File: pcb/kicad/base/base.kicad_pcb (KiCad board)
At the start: 2 copper layers, 58 parts, among them P1 J-Link SWD, P10 CONN_01X02, P11 CONN_01X02, P2 SMA, P3 CONN_01X02, P4 USB Micro B, P5 Button, P6 Button, P7 Button, P8 Button, P9 Button, Q1 IRLML2502, U1 SAMB11G18A-edit, U2 XBee-PRO_900HP, Y1 32.768kHz, Y2 26MHz

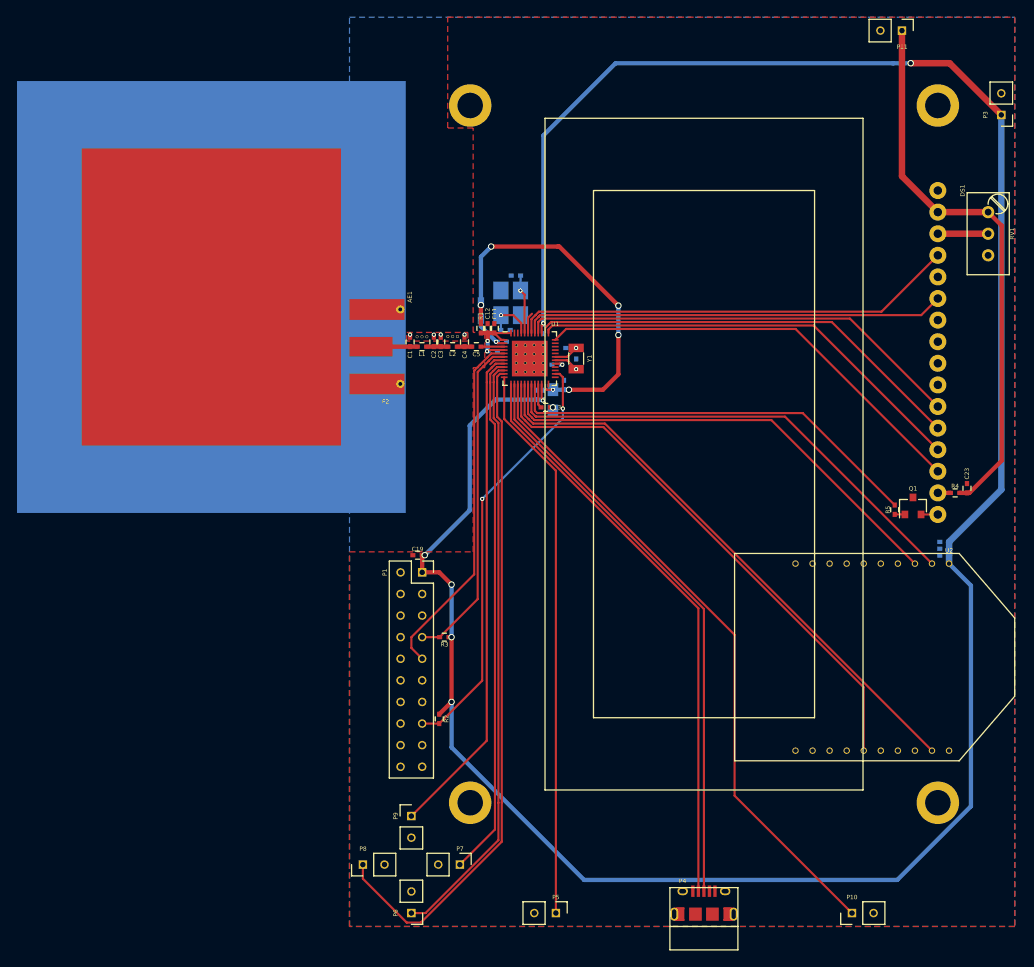
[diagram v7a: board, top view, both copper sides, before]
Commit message: Add ground stitch vias and silk identifiers
Base station layout is finished, and artwork has been generated.
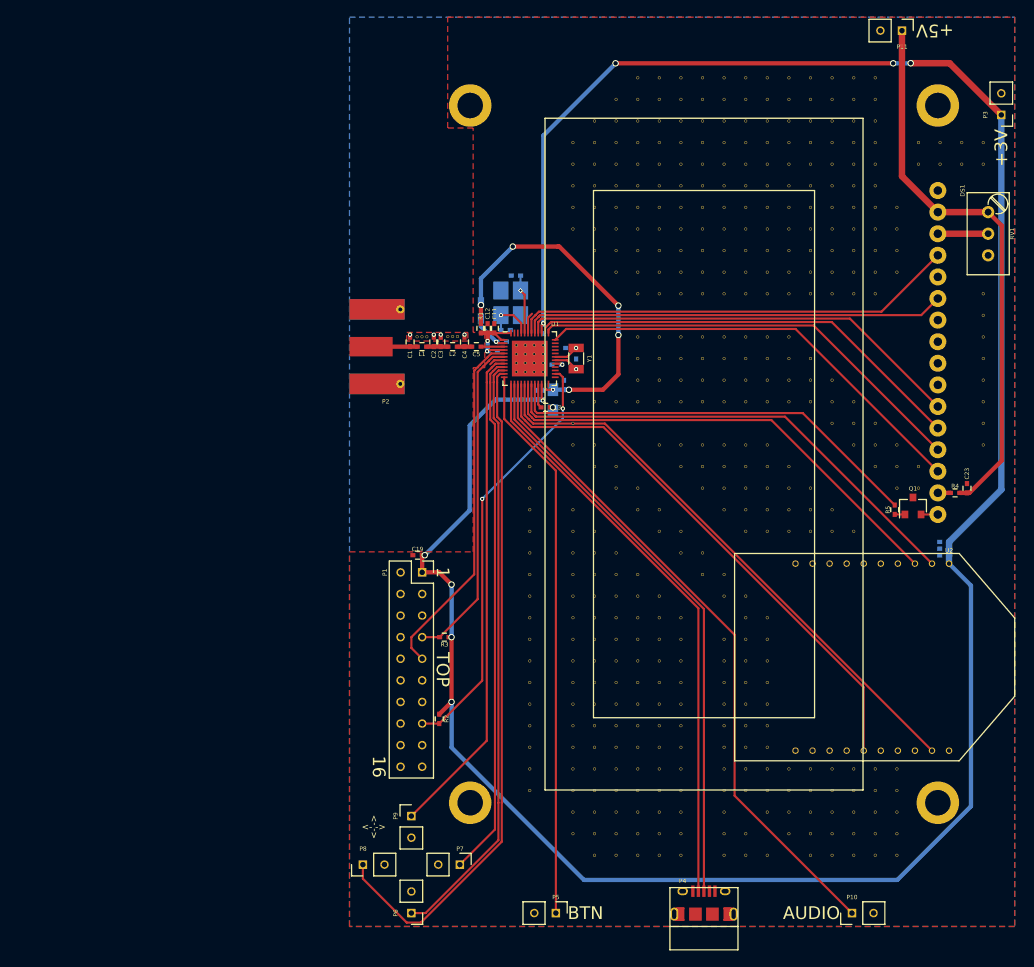
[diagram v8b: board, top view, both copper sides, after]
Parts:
- removed AE1: Antenna_Shield, Antennas:Patch_Antenna_2.4GHz
- added REF**: Via_Stitch_Dia0.356mm_Drill0.254mm, Misc:Via_Stitch_Dia0.356mm_Drill0.254mm, F.Cu at (183.4, 45.3)
- added REF**: Via_Stitch_Dia0.356mm_Drill0.254mm, Misc:Via_Stitch_Dia0.356mm_Drill0.254mm, F.Cu at (183.4, 63.1)
- added REF**: Via_Stitch_Dia0.356mm_Drill0.254mm, Misc:Via_Stitch_Dia0.356mm_Drill0.254mm, F.Cu at (135.1, 88.5)
- added REF**: Via_Stitch_Dia0.356mm_Drill0.254mm, Misc:Via_Stitch_Dia0.356mm_Drill0.254mm, F.Cu at (135.1, 116.5)
- added REF**: Via_Stitch_Dia0.356mm_Drill0.254mm, Misc:Via_Stitch_Dia0.356mm_Drill0.254mm, F.Cu at (135.1, 119.0)
- added REF**: Via_Stitch_Dia0.356mm_Drill0.254mm, Misc:Via_Stitch_Dia0.356mm_Drill0.254mm, F.Cu at (135.1, 121.5)
- added REF**: Via_Stitch_Dia0.356mm_Drill0.254mm, Misc:Via_Stitch_Dia0.356mm_Drill0.254mm, F.Cu at (145.3, 121.5)
- added REF**: Via_Stitch_Dia0.356mm_Drill0.254mm, Misc:Via_Stitch_Dia0.356mm_Drill0.254mm, F.Cu at (142.7, 121.5)
- added REF**: Via_Stitch_Dia0.356mm_Drill0.254mm, Misc:Via_Stitch_Dia0.356mm_Drill0.254mm, F.Cu at (137.6, 121.5)
- added REF**: Via_Stitch_Dia0.356mm_Drill0.254mm, Misc:Via_Stitch_Dia0.356mm_Drill0.254mm, F.Cu at (140.2, 121.5)
- added REF**: Via_Stitch_Dia0.356mm_Drill0.254mm, Misc:Via_Stitch_Dia0.356mm_Drill0.254mm, F.Cu at (145.3, 119.0)
- added REF**: Via_Stitch_Dia0.356mm_Drill0.254mm, Misc:Via_Stitch_Dia0.356mm_Drill0.254mm, F.Cu at (142.7, 119.0)
- added REF**: Via_Stitch_Dia0.356mm_Drill0.254mm, Misc:Via_Stitch_Dia0.356mm_Drill0.254mm, F.Cu at (183.4, 73.3)
- added REF**: Via_Stitch_Dia0.356mm_Drill0.254mm, Misc:Via_Stitch_Dia0.356mm_Drill0.254mm, F.Cu at (137.6, 119.0)
- added REF**: Via_Stitch_Dia0.356mm_Drill0.254mm, Misc:Via_Stitch_Dia0.356mm_Drill0.254mm, F.Cu at (140.2, 119.0)
- added REF**: Via_Stitch_Dia0.356mm_Drill0.254mm, Misc:Via_Stitch_Dia0.356mm_Drill0.254mm, F.Cu at (140.2, 116.5)
- added REF**: Via_Stitch_Dia0.356mm_Drill0.254mm, Misc:Via_Stitch_Dia0.356mm_Drill0.254mm, F.Cu at (137.6, 116.5)
- added REF**: Via_Stitch_Dia0.356mm_Drill0.254mm, Misc:Via_Stitch_Dia0.356mm_Drill0.254mm, F.Cu at (142.7, 116.5)
- added REF**: Via_Stitch_Dia0.356mm_Drill0.254mm, Misc:Via_Stitch_Dia0.356mm_Drill0.254mm, F.Cu at (145.3, 116.5)
- added REF**: Via_Stitch_Dia0.356mm_Drill0.254mm, Misc:Via_Stitch_Dia0.356mm_Drill0.254mm, F.Cu at (147.8, 116.5)
- added REF**: Via_Stitch_Dia0.356mm_Drill0.254mm, Misc:Via_Stitch_Dia0.356mm_Drill0.254mm, F.Cu at (147.8, 119.0)
- added REF**: Via_Stitch_Dia0.356mm_Drill0.254mm, Misc:Via_Stitch_Dia0.356mm_Drill0.254mm, F.Cu at (147.8, 121.5)
- added REF**: Via_Stitch_Dia0.356mm_Drill0.254mm, Misc:Via_Stitch_Dia0.356mm_Drill0.254mm, F.Cu at (147.8, 129.2)
- added REF**: Via_Stitch_Dia0.356mm_Drill0.254mm, Misc:Via_Stitch_Dia0.356mm_Drill0.254mm, F.Cu at (183.4, 75.8)
- added REF**: Via_Stitch_Dia0.356mm_Drill0.254mm, Misc:Via_Stitch_Dia0.356mm_Drill0.254mm, F.Cu at (147.8, 126.6)
- added REF**: Via_Stitch_Dia0.356mm_Drill0.254mm, Misc:Via_Stitch_Dia0.356mm_Drill0.254mm, F.Cu at (147.8, 124.1)
- added REF**: Via_Stitch_Dia0.356mm_Drill0.254mm, Misc:Via_Stitch_Dia0.356mm_Drill0.254mm, F.Cu at (145.3, 124.1)
- added REF**: Via_Stitch_Dia0.356mm_Drill0.254mm, Misc:Via_Stitch_Dia0.356mm_Drill0.254mm, F.Cu at (142.7, 124.1)
- added REF**: Via_Stitch_Dia0.356mm_Drill0.254mm, Misc:Via_Stitch_Dia0.356mm_Drill0.254mm, F.Cu at (137.6, 124.1)
- added REF**: Via_Stitch_Dia0.356mm_Drill0.254mm, Misc:Via_Stitch_Dia0.356mm_Drill0.254mm, F.Cu at (140.2, 124.1)
- added REF**: Via_Stitch_Dia0.356mm_Drill0.254mm, Misc:Via_Stitch_Dia0.356mm_Drill0.254mm, F.Cu at (140.2, 126.6)
- added REF**: Via_Stitch_Dia0.356mm_Drill0.254mm, Misc:Via_Stitch_Dia0.356mm_Drill0.254mm, F.Cu at (137.6, 126.6)
- added REF**: Via_Stitch_Dia0.356mm_Drill0.254mm, Misc:Via_Stitch_Dia0.356mm_Drill0.254mm, F.Cu at (142.7, 126.6)
- added REF**: Via_Stitch_Dia0.356mm_Drill0.254mm, Misc:Via_Stitch_Dia0.356mm_Drill0.254mm, F.Cu at (145.3, 126.6)
- added REF**: Via_Stitch_Dia0.356mm_Drill0.254mm, Misc:Via_Stitch_Dia0.356mm_Drill0.254mm, F.Cu at (183.4, 70.7)
- added REF**: Via_Stitch_Dia0.356mm_Drill0.254mm, Misc:Via_Stitch_Dia0.356mm_Drill0.254mm, F.Cu at (140.2, 129.2)
- added REF**: Via_Stitch_Dia0.356mm_Drill0.254mm, Misc:Via_Stitch_Dia0.356mm_Drill0.254mm, F.Cu at (137.6, 129.2)
- added REF**: Via_Stitch_Dia0.356mm_Drill0.254mm, Misc:Via_Stitch_Dia0.356mm_Drill0.254mm, F.Cu at (142.7, 129.2)
- added REF**: Via_Stitch_Dia0.356mm_Drill0.254mm, Misc:Via_Stitch_Dia0.356mm_Drill0.254mm, F.Cu at (145.3, 129.2)
- added REF**: Via_Stitch_Dia0.356mm_Drill0.254mm, Misc:Via_Stitch_Dia0.356mm_Drill0.254mm, F.Cu at (135.1, 126.6)
- added REF**: Via_Stitch_Dia0.356mm_Drill0.254mm, Misc:Via_Stitch_Dia0.356mm_Drill0.254mm, F.Cu at (135.1, 124.1)
- added REF**: Via_Stitch_Dia0.356mm_Drill0.254mm, Misc:Via_Stitch_Dia0.356mm_Drill0.254mm, F.Cu at (135.1, 108.8)
- added REF**: Via_Stitch_Dia0.356mm_Drill0.254mm, Misc:Via_Stitch_Dia0.356mm_Drill0.254mm, F.Cu at (135.1, 111.4)
- added REF**: Via_Stitch_Dia0.356mm_Drill0.254mm, Misc:Via_Stitch_Dia0.356mm_Drill0.254mm, F.Cu at (135.1, 113.9)
- added REF**: Via_Stitch_Dia0.356mm_Drill0.254mm, Misc:Via_Stitch_Dia0.356mm_Drill0.254mm, F.Cu at (145.3, 113.9)
- added REF**: Via_Stitch_Dia0.356mm_Drill0.254mm, Misc:Via_Stitch_Dia0.356mm_Drill0.254mm, F.Cu at (183.4, 68.2)
- added REF**: Via_Stitch_Dia0.356mm_Drill0.254mm, Misc:Via_Stitch_Dia0.356mm_Drill0.254mm, F.Cu at (142.7, 113.9)
- added REF**: Via_Stitch_Dia0.356mm_Drill0.254mm, Misc:Via_Stitch_Dia0.356mm_Drill0.254mm, F.Cu at (137.6, 113.9)
- added REF**: Via_Stitch_Dia0.356mm_Drill0.254mm, Misc:Via_Stitch_Dia0.356mm_Drill0.254mm, F.Cu at (140.2, 113.9)
- added REF**: Via_Stitch_Dia0.356mm_Drill0.254mm, Misc:Via_Stitch_Dia0.356mm_Drill0.254mm, F.Cu at (145.3, 111.4)
- added REF**: Via_Stitch_Dia0.356mm_Drill0.254mm, Misc:Via_Stitch_Dia0.356mm_Drill0.254mm, F.Cu at (142.7, 111.4)
- added REF**: Via_Stitch_Dia0.356mm_Drill0.254mm, Misc:Via_Stitch_Dia0.356mm_Drill0.254mm, F.Cu at (137.6, 111.4)
- added REF**: Via_Stitch_Dia0.356mm_Drill0.254mm, Misc:Via_Stitch_Dia0.356mm_Drill0.254mm, F.Cu at (140.2, 111.4)
- added REF**: Via_Stitch_Dia0.356mm_Drill0.254mm, Misc:Via_Stitch_Dia0.356mm_Drill0.254mm, F.Cu at (140.2, 108.8)
- added REF**: Via_Stitch_Dia0.356mm_Drill0.254mm, Misc:Via_Stitch_Dia0.356mm_Drill0.254mm, F.Cu at (137.6, 108.8)
- added REF**: Via_Stitch_Dia0.356mm_Drill0.254mm, Misc:Via_Stitch_Dia0.356mm_Drill0.254mm, F.Cu at (142.7, 108.8)
- added REF**: Via_Stitch_Dia0.356mm_Drill0.254mm, Misc:Via_Stitch_Dia0.356mm_Drill0.254mm, F.Cu at (183.4, 78.4)
- added REF**: Via_Stitch_Dia0.356mm_Drill0.254mm, Misc:Via_Stitch_Dia0.356mm_Drill0.254mm, F.Cu at (145.3, 108.8)
- added REF**: Via_Stitch_Dia0.356mm_Drill0.254mm, Misc:Via_Stitch_Dia0.356mm_Drill0.254mm, F.Cu at (147.8, 108.8)
- added REF**: Via_Stitch_Dia0.356mm_Drill0.254mm, Misc:Via_Stitch_Dia0.356mm_Drill0.254mm, F.Cu at (147.8, 111.4)
- added REF**: Via_Stitch_Dia0.356mm_Drill0.254mm, Misc:Via_Stitch_Dia0.356mm_Drill0.254mm, F.Cu at (147.8, 113.9)
- added REF**: Via_Stitch_Dia0.356mm_Drill0.254mm, Misc:Via_Stitch_Dia0.356mm_Drill0.254mm, F.Cu at (147.8, 106.3)
- added REF**: Via_Stitch_Dia0.356mm_Drill0.254mm, Misc:Via_Stitch_Dia0.356mm_Drill0.254mm, F.Cu at (147.8, 103.8)
- added REF**: Via_Stitch_Dia0.356mm_Drill0.254mm, Misc:Via_Stitch_Dia0.356mm_Drill0.254mm, F.Cu at (147.8, 101.2)
- added REF**: Via_Stitch_Dia0.356mm_Drill0.254mm, Misc:Via_Stitch_Dia0.356mm_Drill0.254mm, F.Cu at (135.1, 78.4)
- added REF**: Via_Stitch_Dia0.356mm_Drill0.254mm, Misc:Via_Stitch_Dia0.356mm_Drill0.254mm, F.Cu at (135.1, 80.9)
- added REF**: Via_Stitch_Dia0.356mm_Drill0.254mm, Misc:Via_Stitch_Dia0.356mm_Drill0.254mm, F.Cu at (137.6, 80.9)
- added REF**: Via_Stitch_Dia0.356mm_Drill0.254mm, Misc:Via_Stitch_Dia0.356mm_Drill0.254mm, F.Cu at (183.4, 80.9)
- added REF**: Via_Stitch_Dia0.356mm_Drill0.254mm, Misc:Via_Stitch_Dia0.356mm_Drill0.254mm, F.Cu at (137.6, 83.4)
- added REF**: Via_Stitch_Dia0.356mm_Drill0.254mm, Misc:Via_Stitch_Dia0.356mm_Drill0.254mm, F.Cu at (142.7, 88.5)
- added REF**: Via_Stitch_Dia0.356mm_Drill0.254mm, Misc:Via_Stitch_Dia0.356mm_Drill0.254mm, F.Cu at (142.7, 86.0)
- added REF**: Via_Stitch_Dia0.356mm_Drill0.254mm, Misc:Via_Stitch_Dia0.356mm_Drill0.254mm, F.Cu at (140.2, 86.0)
- added REF**: Via_Stitch_Dia0.356mm_Drill0.254mm, Misc:Via_Stitch_Dia0.356mm_Drill0.254mm, F.Cu at (140.2, 83.4)
- added REF**: Via_Stitch_Dia0.356mm_Drill0.254mm, Misc:Via_Stitch_Dia0.356mm_Drill0.254mm, F.Cu at (163.0, 88.5)
- added REF**: Via_Stitch_Dia0.356mm_Drill0.254mm, Misc:Via_Stitch_Dia0.356mm_Drill0.254mm, F.Cu at (165.6, 88.5)
- added REF**: Via_Stitch_Dia0.356mm_Drill0.254mm, Misc:Via_Stitch_Dia0.356mm_Drill0.254mm, F.Cu at (165.6, 91.1)
- added REF**: Via_Stitch_Dia0.356mm_Drill0.254mm, Misc:Via_Stitch_Dia0.356mm_Drill0.254mm, F.Cu at (163.0, 91.1)
- added REF**: Via_Stitch_Dia0.356mm_Drill0.254mm, Misc:Via_Stitch_Dia0.356mm_Drill0.254mm, F.Cu at (163.0, 86.0)
- added REF**: Via_Stitch_Dia0.356mm_Drill0.254mm, Misc:Via_Stitch_Dia0.356mm_Drill0.254mm, F.Cu at (173.2, 129.2)
- added REF**: Via_Stitch_Dia0.356mm_Drill0.254mm, Misc:Via_Stitch_Dia0.356mm_Drill0.254mm, F.Cu at (158.0, 83.4)
- added REF**: Via_Stitch_Dia0.356mm_Drill0.254mm, Misc:Via_Stitch_Dia0.356mm_Drill0.254mm, F.Cu at (160.5, 83.4)
- added REF**: Via_Stitch_Dia0.356mm_Drill0.254mm, Misc:Via_Stitch_Dia0.356mm_Drill0.254mm, F.Cu at (160.5, 86.0)
- added REF**: Via_Stitch_Dia0.356mm_Drill0.254mm, Misc:Via_Stitch_Dia0.356mm_Drill0.254mm, F.Cu at (158.0, 86.0)
- added REF**: Via_Stitch_Dia0.356mm_Drill0.254mm, Misc:Via_Stitch_Dia0.356mm_Drill0.254mm, F.Cu at (158.0, 91.1)
- added REF**: Via_Stitch_Dia0.356mm_Drill0.254mm, Misc:Via_Stitch_Dia0.356mm_Drill0.254mm, F.Cu at (160.5, 91.1)
- added REF**: Via_Stitch_Dia0.356mm_Drill0.254mm, Misc:Via_Stitch_Dia0.356mm_Drill0.254mm, F.Cu at (160.5, 88.5)
- added REF**: Via_Stitch_Dia0.356mm_Drill0.254mm, Misc:Via_Stitch_Dia0.356mm_Drill0.254mm, F.Cu at (158.0, 88.5)
- added REF**: Via_Stitch_Dia0.356mm_Drill0.254mm, Misc:Via_Stitch_Dia0.356mm_Drill0.254mm, F.Cu at (158.0, 80.9)
- added REF**: Via_Stitch_Dia0.356mm_Drill0.254mm, Misc:Via_Stitch_Dia0.356mm_Drill0.254mm, F.Cu at (147.8, 80.9)
- added REF**: Via_Stitch_Dia0.356mm_Drill0.254mm, Misc:Via_Stitch_Dia0.356mm_Drill0.254mm, F.Cu at (165.6, 129.2)
- added REF**: Via_Stitch_Dia0.356mm_Drill0.254mm, Misc:Via_Stitch_Dia0.356mm_Drill0.254mm, F.Cu at (145.3, 80.9)
- added REF**: Via_Stitch_Dia0.356mm_Drill0.254mm, Misc:Via_Stitch_Dia0.356mm_Drill0.254mm, F.Cu at (152.9, 80.9)
- added REF**: Via_Stitch_Dia0.356mm_Drill0.254mm, Misc:Via_Stitch_Dia0.356mm_Drill0.254mm, F.Cu at (150.3, 80.9)
- added REF**: Via_Stitch_Dia0.356mm_Drill0.254mm, Misc:Via_Stitch_Dia0.356mm_Drill0.254mm, F.Cu at (155.4, 80.9)
- added REF**: Via_Stitch_Dia0.356mm_Drill0.254mm, Misc:Via_Stitch_Dia0.356mm_Drill0.254mm, F.Cu at (145.3, 88.5)
- added REF**: Via_Stitch_Dia0.356mm_Drill0.254mm, Misc:Via_Stitch_Dia0.356mm_Drill0.254mm, F.Cu at (152.9, 88.5)
- added REF**: Via_Stitch_Dia0.356mm_Drill0.254mm, Misc:Via_Stitch_Dia0.356mm_Drill0.254mm, F.Cu at (155.4, 88.5)
- added REF**: Via_Stitch_Dia0.356mm_Drill0.254mm, Misc:Via_Stitch_Dia0.356mm_Drill0.254mm, F.Cu at (155.4, 91.1)
- added REF**: Via_Stitch_Dia0.356mm_Drill0.254mm, Misc:Via_Stitch_Dia0.356mm_Drill0.254mm, F.Cu at (145.3, 91.1)
- added REF**: Via_Stitch_Dia0.356mm_Drill0.254mm, Misc:Via_Stitch_Dia0.356mm_Drill0.254mm, F.Cu at (147.8, 91.1)
- added REF**: Via_Stitch_Dia0.356mm_Drill0.254mm, Misc:Via_Stitch_Dia0.356mm_Drill0.254mm, F.Cu at (163.0, 129.2)
- added REF**: Via_Stitch_Dia0.356mm_Drill0.254mm, Misc:Via_Stitch_Dia0.356mm_Drill0.254mm, F.Cu at (152.9, 86.0)
- added REF**: Via_Stitch_Dia0.356mm_Drill0.254mm, Misc:Via_Stitch_Dia0.356mm_Drill0.254mm, F.Cu at (150.3, 86.0)
- added REF**: Via_Stitch_Dia0.356mm_Drill0.254mm, Misc:Via_Stitch_Dia0.356mm_Drill0.254mm, F.Cu at (155.4, 86.0)
- added REF**: Via_Stitch_Dia0.356mm_Drill0.254mm, Misc:Via_Stitch_Dia0.356mm_Drill0.254mm, F.Cu at (155.4, 83.4)
- added REF**: Via_Stitch_Dia0.356mm_Drill0.254mm, Misc:Via_Stitch_Dia0.356mm_Drill0.254mm, F.Cu at (150.3, 83.4)
- added REF**: Via_Stitch_Dia0.356mm_Drill0.254mm, Misc:Via_Stitch_Dia0.356mm_Drill0.254mm, F.Cu at (152.9, 83.4)
- added REF**: Via_Stitch_Dia0.356mm_Drill0.254mm, Misc:Via_Stitch_Dia0.356mm_Drill0.254mm, F.Cu at (147.8, 83.4)
- added REF**: Via_Stitch_Dia0.356mm_Drill0.254mm, Misc:Via_Stitch_Dia0.356mm_Drill0.254mm, F.Cu at (150.3, 93.6)
- added REF**: Via_Stitch_Dia0.356mm_Drill0.254mm, Misc:Via_Stitch_Dia0.356mm_Drill0.254mm, F.Cu at (147.8, 93.6)
- added REF**: Via_Stitch_Dia0.356mm_Drill0.254mm, Misc:Via_Stitch_Dia0.356mm_Drill0.254mm, F.Cu at (137.6, 93.6)
- added REF**: Via_Stitch_Dia0.356mm_Drill0.254mm, Misc:Via_Stitch_Dia0.356mm_Drill0.254mm, F.Cu at (180.8, 45.3)
- added REF**: Via_Stitch_Dia0.356mm_Drill0.254mm, Misc:Via_Stitch_Dia0.356mm_Drill0.254mm, F.Cu at (168.1, 129.2)
- added REF**: Via_Stitch_Dia0.356mm_Drill0.254mm, Misc:Via_Stitch_Dia0.356mm_Drill0.254mm, F.Cu at (140.2, 93.6)
- added REF**: Via_Stitch_Dia0.356mm_Drill0.254mm, Misc:Via_Stitch_Dia0.356mm_Drill0.254mm, F.Cu at (137.6, 91.1)
- added REF**: Via_Stitch_Dia0.356mm_Drill0.254mm, Misc:Via_Stitch_Dia0.356mm_Drill0.254mm, F.Cu at (145.3, 101.2)
- added REF**: Via_Stitch_Dia0.356mm_Drill0.254mm, Misc:Via_Stitch_Dia0.356mm_Drill0.254mm, F.Cu at (142.7, 101.2)
- added REF**: Via_Stitch_Dia0.356mm_Drill0.254mm, Misc:Via_Stitch_Dia0.356mm_Drill0.254mm, F.Cu at (137.6, 101.2)
- added REF**: Via_Stitch_Dia0.356mm_Drill0.254mm, Misc:Via_Stitch_Dia0.356mm_Drill0.254mm, F.Cu at (140.2, 101.2)
- added REF**: Via_Stitch_Dia0.356mm_Drill0.254mm, Misc:Via_Stitch_Dia0.356mm_Drill0.254mm, F.Cu at (140.2, 103.8)
- added REF**: Via_Stitch_Dia0.356mm_Drill0.254mm, Misc:Via_Stitch_Dia0.356mm_Drill0.254mm, F.Cu at (137.6, 103.8)
- added REF**: Via_Stitch_Dia0.356mm_Drill0.254mm, Misc:Via_Stitch_Dia0.356mm_Drill0.254mm, F.Cu at (142.7, 103.8)
- added REF**: Via_Stitch_Dia0.356mm_Drill0.254mm, Misc:Via_Stitch_Dia0.356mm_Drill0.254mm, F.Cu at (145.3, 103.8)
- added REF**: Via_Stitch_Dia0.356mm_Drill0.254mm, Misc:Via_Stitch_Dia0.356mm_Drill0.254mm, F.Cu at (170.7, 129.2)
- added REF**: Via_Stitch_Dia0.356mm_Drill0.254mm, Misc:Via_Stitch_Dia0.356mm_Drill0.254mm, F.Cu at (145.3, 98.7)
- added REF**: Via_Stitch_Dia0.356mm_Drill0.254mm, Misc:Via_Stitch_Dia0.356mm_Drill0.254mm, F.Cu at (142.7, 98.7)
- added REF**: Via_Stitch_Dia0.356mm_Drill0.254mm, Misc:Via_Stitch_Dia0.356mm_Drill0.254mm, F.Cu at (137.6, 98.7)
- added REF**: Via_Stitch_Dia0.356mm_Drill0.254mm, Misc:Via_Stitch_Dia0.356mm_Drill0.254mm, F.Cu at (140.2, 98.7)
- added REF**: Via_Stitch_Dia0.356mm_Drill0.254mm, Misc:Via_Stitch_Dia0.356mm_Drill0.254mm, F.Cu at (140.2, 96.1)
- added REF**: Via_Stitch_Dia0.356mm_Drill0.254mm, Misc:Via_Stitch_Dia0.356mm_Drill0.254mm, F.Cu at (137.6, 96.1)
- added REF**: Via_Stitch_Dia0.356mm_Drill0.254mm, Misc:Via_Stitch_Dia0.356mm_Drill0.254mm, F.Cu at (142.7, 96.1)
- added REF**: Via_Stitch_Dia0.356mm_Drill0.254mm, Misc:Via_Stitch_Dia0.356mm_Drill0.254mm, F.Cu at (140.2, 106.3)
- added REF**: Via_Stitch_Dia0.356mm_Drill0.254mm, Misc:Via_Stitch_Dia0.356mm_Drill0.254mm, F.Cu at (137.6, 106.3)
- added REF**: Via_Stitch_Dia0.356mm_Drill0.254mm, Misc:Via_Stitch_Dia0.356mm_Drill0.254mm, F.Cu at (142.7, 106.3)
- added REF**: Via_Stitch_Dia0.356mm_Drill0.254mm, Misc:Via_Stitch_Dia0.356mm_Drill0.254mm, F.Cu at (160.5, 124.1)
- added REF**: Via_Stitch_Dia0.356mm_Drill0.254mm, Misc:Via_Stitch_Dia0.356mm_Drill0.254mm, F.Cu at (145.3, 106.3)
- added REF**: Via_Stitch_Dia0.356mm_Drill0.254mm, Misc:Via_Stitch_Dia0.356mm_Drill0.254mm, F.Cu at (135.1, 106.3)
- added REF**: Via_Stitch_Dia0.356mm_Drill0.254mm, Misc:Via_Stitch_Dia0.356mm_Drill0.254mm, F.Cu at (135.1, 96.1)
- added REF**: Via_Stitch_Dia0.356mm_Drill0.254mm, Misc:Via_Stitch_Dia0.356mm_Drill0.254mm, F.Cu at (135.1, 98.7)
- added REF**: Via_Stitch_Dia0.356mm_Drill0.254mm, Misc:Via_Stitch_Dia0.356mm_Drill0.254mm, F.Cu at (135.1, 103.8)
- added REF**: Via_Stitch_Dia0.356mm_Drill0.254mm, Misc:Via_Stitch_Dia0.356mm_Drill0.254mm, F.Cu at (135.1, 101.2)
- added REF**: Via_Stitch_Dia0.356mm_Drill0.254mm, Misc:Via_Stitch_Dia0.356mm_Drill0.254mm, F.Cu at (135.1, 91.1)
- added REF**: Via_Stitch_Dia0.356mm_Drill0.254mm, Misc:Via_Stitch_Dia0.356mm_Drill0.254mm, F.Cu at (135.1, 93.6)
- added REF**: Via_Stitch_Dia0.356mm_Drill0.254mm, Misc:Via_Stitch_Dia0.356mm_Drill0.254mm, F.Cu at (175.7, 86.0)
- added REF**: Via_Stitch_Dia0.356mm_Drill0.254mm, Misc:Via_Stitch_Dia0.356mm_Drill0.254mm, F.Cu at (173.2, 86.0)
- added REF**: Via_Stitch_Dia0.356mm_Drill0.254mm, Misc:Via_Stitch_Dia0.356mm_Drill0.254mm, F.Cu at (160.5, 126.6)
- added REF**: Via_Stitch_Dia0.356mm_Drill0.254mm, Misc:Via_Stitch_Dia0.356mm_Drill0.254mm, F.Cu at (175.7, 83.4)
- added REF**: Via_Stitch_Dia0.356mm_Drill0.254mm, Misc:Via_Stitch_Dia0.356mm_Drill0.254mm, F.Cu at (173.2, 83.4)
- added REF**: Via_Stitch_Dia0.356mm_Drill0.254mm, Misc:Via_Stitch_Dia0.356mm_Drill0.254mm, F.Cu at (165.6, 73.3)
- added REF**: Via_Stitch_Dia0.356mm_Drill0.254mm, Misc:Via_Stitch_Dia0.356mm_Drill0.254mm, F.Cu at (168.1, 75.8)
- added REF**: Via_Stitch_Dia0.356mm_Drill0.254mm, Misc:Via_Stitch_Dia0.356mm_Drill0.254mm, F.Cu at (165.6, 75.8)
- added REF**: Via_Stitch_Dia0.356mm_Drill0.254mm, Misc:Via_Stitch_Dia0.356mm_Drill0.254mm, F.Cu at (165.6, 78.4)
- added REF**: Via_Stitch_Dia0.356mm_Drill0.254mm, Misc:Via_Stitch_Dia0.356mm_Drill0.254mm, F.Cu at (168.1, 78.4)
- added REF**: Via_Stitch_Dia0.356mm_Drill0.254mm, Misc:Via_Stitch_Dia0.356mm_Drill0.254mm, F.Cu at (170.7, 78.4)
- added REF**: Via_Stitch_Dia0.356mm_Drill0.254mm, Misc:Via_Stitch_Dia0.356mm_Drill0.254mm, F.Cu at (168.1, 80.9)
- added REF**: Via_Stitch_Dia0.356mm_Drill0.254mm, Misc:Via_Stitch_Dia0.356mm_Drill0.254mm, F.Cu at (170.7, 80.9)
- added REF**: Via_Stitch_Dia0.356mm_Drill0.254mm, Misc:Via_Stitch_Dia0.356mm_Drill0.254mm, F.Cu at (170.7, 126.6)
- added REF**: Via_Stitch_Dia0.356mm_Drill0.254mm, Misc:Via_Stitch_Dia0.356mm_Drill0.254mm, F.Cu at (173.2, 80.9)
- added REF**: Via_Stitch_Dia0.356mm_Drill0.254mm, Misc:Via_Stitch_Dia0.356mm_Drill0.254mm, F.Cu at (170.7, 83.4)
- added REF**: Via_Stitch_Dia0.356mm_Drill0.254mm, Misc:Via_Stitch_Dia0.356mm_Drill0.254mm, F.Cu at (140.2, 75.8)
- added REF**: Via_Stitch_Dia0.356mm_Drill0.254mm, Misc:Via_Stitch_Dia0.356mm_Drill0.254mm, F.Cu at (137.6, 75.8)
- added REF**: Via_Stitch_Dia0.356mm_Drill0.254mm, Misc:Via_Stitch_Dia0.356mm_Drill0.254mm, F.Cu at (135.1, 75.8)
- added REF**: Via_Stitch_Dia0.356mm_Drill0.254mm, Misc:Via_Stitch_Dia0.356mm_Drill0.254mm, F.Cu at (158.0, 75.8)
- added REF**: Via_Stitch_Dia0.356mm_Drill0.254mm, Misc:Via_Stitch_Dia0.356mm_Drill0.254mm, F.Cu at (155.4, 75.8)
- added REF**: Via_Stitch_Dia0.356mm_Drill0.254mm, Misc:Via_Stitch_Dia0.356mm_Drill0.254mm, F.Cu at (150.3, 75.8)
- added REF**: Via_Stitch_Dia0.356mm_Drill0.254mm, Misc:Via_Stitch_Dia0.356mm_Drill0.254mm, F.Cu at (152.9, 75.8)
- added REF**: Via_Stitch_Dia0.356mm_Drill0.254mm, Misc:Via_Stitch_Dia0.356mm_Drill0.254mm, F.Cu at (142.7, 75.8)
- added REF**: Via_Stitch_Dia0.356mm_Drill0.254mm, Misc:Via_Stitch_Dia0.356mm_Drill0.254mm, F.Cu at (168.1, 126.6)
- added REF**: Via_Stitch_Dia0.356mm_Drill0.254mm, Misc:Via_Stitch_Dia0.356mm_Drill0.254mm, F.Cu at (145.3, 75.8)
- added REF**: Via_Stitch_Dia0.356mm_Drill0.254mm, Misc:Via_Stitch_Dia0.356mm_Drill0.254mm, F.Cu at (147.8, 75.8)
- added REF**: Via_Stitch_Dia0.356mm_Drill0.254mm, Misc:Via_Stitch_Dia0.356mm_Drill0.254mm, F.Cu at (160.5, 75.8)
- added REF**: Via_Stitch_Dia0.356mm_Drill0.254mm, Misc:Via_Stitch_Dia0.356mm_Drill0.254mm, F.Cu at (163.0, 75.8)
- added REF**: Via_Stitch_Dia0.356mm_Drill0.254mm, Misc:Via_Stitch_Dia0.356mm_Drill0.254mm, F.Cu at (163.0, 70.7)
- added REF**: Via_Stitch_Dia0.356mm_Drill0.254mm, Misc:Via_Stitch_Dia0.356mm_Drill0.254mm, F.Cu at (163.0, 73.3)
- added REF**: Via_Stitch_Dia0.356mm_Drill0.254mm, Misc:Via_Stitch_Dia0.356mm_Drill0.254mm, F.Cu at (158.0, 68.2)
- added REF**: Via_Stitch_Dia0.356mm_Drill0.254mm, Misc:Via_Stitch_Dia0.356mm_Drill0.254mm, F.Cu at (155.4, 68.2)
- added REF**: Via_Stitch_Dia0.356mm_Drill0.254mm, Misc:Via_Stitch_Dia0.356mm_Drill0.254mm, F.Cu at (150.3, 68.2)
- added REF**: Via_Stitch_Dia0.356mm_Drill0.254mm, Misc:Via_Stitch_Dia0.356mm_Drill0.254mm, F.Cu at (152.9, 68.2)
- added REF**: Via_Stitch_Dia0.356mm_Drill0.254mm, Misc:Via_Stitch_Dia0.356mm_Drill0.254mm, F.Cu at (163.0, 126.6)
- added REF**: Via_Stitch_Dia0.356mm_Drill0.254mm, Misc:Via_Stitch_Dia0.356mm_Drill0.254mm, F.Cu at (142.7, 68.2)
- added REF**: Via_Stitch_Dia0.356mm_Drill0.254mm, Misc:Via_Stitch_Dia0.356mm_Drill0.254mm, F.Cu at (145.3, 68.2)
- added REF**: Via_Stitch_Dia0.356mm_Drill0.254mm, Misc:Via_Stitch_Dia0.356mm_Drill0.254mm, F.Cu at (147.8, 68.2)
- added REF**: Via_Stitch_Dia0.356mm_Drill0.254mm, Misc:Via_Stitch_Dia0.356mm_Drill0.254mm, F.Cu at (160.5, 68.2)
- added REF**: Via_Stitch_Dia0.356mm_Drill0.254mm, Misc:Via_Stitch_Dia0.356mm_Drill0.254mm, F.Cu at (160.5, 73.3)
- added REF**: Via_Stitch_Dia0.356mm_Drill0.254mm, Misc:Via_Stitch_Dia0.356mm_Drill0.254mm, F.Cu at (147.8, 73.3)
- added REF**: Via_Stitch_Dia0.356mm_Drill0.254mm, Misc:Via_Stitch_Dia0.356mm_Drill0.254mm, F.Cu at (145.3, 73.3)
- added REF**: Via_Stitch_Dia0.356mm_Drill0.254mm, Misc:Via_Stitch_Dia0.356mm_Drill0.254mm, F.Cu at (142.7, 73.3)
- added REF**: Via_Stitch_Dia0.356mm_Drill0.254mm, Misc:Via_Stitch_Dia0.356mm_Drill0.254mm, F.Cu at (152.9, 73.3)
- added REF**: Via_Stitch_Dia0.356mm_Drill0.254mm, Misc:Via_Stitch_Dia0.356mm_Drill0.254mm, F.Cu at (150.3, 73.3)
- added REF**: Via_Stitch_Dia0.356mm_Drill0.254mm, Misc:Via_Stitch_Dia0.356mm_Drill0.254mm, F.Cu at (165.6, 126.6)
- added REF**: Via_Stitch_Dia0.356mm_Drill0.254mm, Misc:Via_Stitch_Dia0.356mm_Drill0.254mm, F.Cu at (155.4, 73.3)
- added REF**: Via_Stitch_Dia0.356mm_Drill0.254mm, Misc:Via_Stitch_Dia0.356mm_Drill0.254mm, F.Cu at (158.0, 73.3)
- added REF**: Via_Stitch_Dia0.356mm_Drill0.254mm, Misc:Via_Stitch_Dia0.356mm_Drill0.254mm, F.Cu at (158.0, 70.7)
- added REF**: Via_Stitch_Dia0.356mm_Drill0.254mm, Misc:Via_Stitch_Dia0.356mm_Drill0.254mm, F.Cu at (155.4, 70.7)
- added REF**: Via_Stitch_Dia0.356mm_Drill0.254mm, Misc:Via_Stitch_Dia0.356mm_Drill0.254mm, F.Cu at (150.3, 70.7)
- added REF**: Via_Stitch_Dia0.356mm_Drill0.254mm, Misc:Via_Stitch_Dia0.356mm_Drill0.254mm, F.Cu at (152.9, 70.7)
- added REF**: Via_Stitch_Dia0.356mm_Drill0.254mm, Misc:Via_Stitch_Dia0.356mm_Drill0.254mm, F.Cu at (142.7, 70.7)
- added REF**: Via_Stitch_Dia0.356mm_Drill0.254mm, Misc:Via_Stitch_Dia0.356mm_Drill0.254mm, F.Cu at (145.3, 70.7)
- added REF**: Via_Stitch_Dia0.356mm_Drill0.254mm, Misc:Via_Stitch_Dia0.356mm_Drill0.254mm, F.Cu at (147.8, 70.7)
- added REF**: Via_Stitch_Dia0.356mm_Drill0.254mm, Misc:Via_Stitch_Dia0.356mm_Drill0.254mm, F.Cu at (160.5, 70.7)
- added REF**: Via_Stitch_Dia0.356mm_Drill0.254mm, Misc:Via_Stitch_Dia0.356mm_Drill0.254mm, F.Cu at (165.6, 124.1)
- added REF**: Via_Stitch_Dia0.356mm_Drill0.254mm, Misc:Via_Stitch_Dia0.356mm_Drill0.254mm, F.Cu at (135.1, 45.3)
- added REF**: Via_Stitch_Dia0.356mm_Drill0.254mm, Misc:Via_Stitch_Dia0.356mm_Drill0.254mm, F.Cu at (137.6, 45.3)
- added REF**: Via_Stitch_Dia0.356mm_Drill0.254mm, Misc:Via_Stitch_Dia0.356mm_Drill0.254mm, F.Cu at (137.6, 42.8)
- added REF**: Via_Stitch_Dia0.356mm_Drill0.254mm, Misc:Via_Stitch_Dia0.356mm_Drill0.254mm, F.Cu at (135.1, 53.0)
- added REF**: Via_Stitch_Dia0.356mm_Drill0.254mm, Misc:Via_Stitch_Dia0.356mm_Drill0.254mm, F.Cu at (137.6, 53.0)
- added REF**: Via_Stitch_Dia0.356mm_Drill0.254mm, Misc:Via_Stitch_Dia0.356mm_Drill0.254mm, F.Cu at (137.6, 55.5)
- added REF**: Via_Stitch_Dia0.356mm_Drill0.254mm, Misc:Via_Stitch_Dia0.356mm_Drill0.254mm, F.Cu at (135.1, 55.5)
- added REF**: Via_Stitch_Dia0.356mm_Drill0.254mm, Misc:Via_Stitch_Dia0.356mm_Drill0.254mm, F.Cu at (135.1, 50.4)
- added REF**: Via_Stitch_Dia0.356mm_Drill0.254mm, Misc:Via_Stitch_Dia0.356mm_Drill0.254mm, F.Cu at (137.6, 50.4)
- added REF**: Via_Stitch_Dia0.356mm_Drill0.254mm, Misc:Via_Stitch_Dia0.356mm_Drill0.254mm, F.Cu at (137.6, 47.9)
- added REF**: Via_Stitch_Dia0.356mm_Drill0.254mm, Misc:Via_Stitch_Dia0.356mm_Drill0.254mm, F.Cu at (163.0, 124.1)
- added REF**: Via_Stitch_Dia0.356mm_Drill0.254mm, Misc:Via_Stitch_Dia0.356mm_Drill0.254mm, F.Cu at (135.1, 47.9)
- added REF**: Via_Stitch_Dia0.356mm_Drill0.254mm, Misc:Via_Stitch_Dia0.356mm_Drill0.254mm, F.Cu at (137.6, 58.0)
- added REF**: Via_Stitch_Dia0.356mm_Drill0.254mm, Misc:Via_Stitch_Dia0.356mm_Drill0.254mm, F.Cu at (173.2, 53.0)
- added REF**: Via_Stitch_Dia0.356mm_Drill0.254mm, Misc:Via_Stitch_Dia0.356mm_Drill0.254mm, F.Cu at (173.2, 55.5)
- added REF**: Via_Stitch_Dia0.356mm_Drill0.254mm, Misc:Via_Stitch_Dia0.356mm_Drill0.254mm, F.Cu at (173.2, 58.0)
- added REF**: Via_Stitch_Dia0.356mm_Drill0.254mm, Misc:Via_Stitch_Dia0.356mm_Drill0.254mm, F.Cu at (173.2, 60.6)
- added REF**: Via_Stitch_Dia0.356mm_Drill0.254mm, Misc:Via_Stitch_Dia0.356mm_Drill0.254mm, F.Cu at (170.7, 60.6)
- added REF**: Via_Stitch_Dia0.356mm_Drill0.254mm, Misc:Via_Stitch_Dia0.356mm_Drill0.254mm, F.Cu at (168.1, 60.6)
- added REF**: Via_Stitch_Dia0.356mm_Drill0.254mm, Misc:Via_Stitch_Dia0.356mm_Drill0.254mm, F.Cu at (165.6, 60.6)
- added REF**: Via_Stitch_Dia0.356mm_Drill0.254mm, Misc:Via_Stitch_Dia0.356mm_Drill0.254mm, F.Cu at (160.5, 60.6)
- added REF**: Via_Stitch_Dia0.356mm_Drill0.254mm, Misc:Via_Stitch_Dia0.356mm_Drill0.254mm, F.Cu at (178.3, 45.3)
- added REF**: Via_Stitch_Dia0.356mm_Drill0.254mm, Misc:Via_Stitch_Dia0.356mm_Drill0.254mm, F.Cu at (168.1, 124.1)
- added REF**: Via_Stitch_Dia0.356mm_Drill0.254mm, Misc:Via_Stitch_Dia0.356mm_Drill0.254mm, F.Cu at (163.0, 60.6)
- added REF**: Via_Stitch_Dia0.356mm_Drill0.254mm, Misc:Via_Stitch_Dia0.356mm_Drill0.254mm, F.Cu at (147.8, 60.6)
- added REF**: Via_Stitch_Dia0.356mm_Drill0.254mm, Misc:Via_Stitch_Dia0.356mm_Drill0.254mm, F.Cu at (145.3, 60.6)
- added REF**: Via_Stitch_Dia0.356mm_Drill0.254mm, Misc:Via_Stitch_Dia0.356mm_Drill0.254mm, F.Cu at (140.2, 60.6)
- added REF**: Via_Stitch_Dia0.356mm_Drill0.254mm, Misc:Via_Stitch_Dia0.356mm_Drill0.254mm, F.Cu at (142.7, 60.6)
- added REF**: Via_Stitch_Dia0.356mm_Drill0.254mm, Misc:Via_Stitch_Dia0.356mm_Drill0.254mm, F.Cu at (152.9, 60.6)
- added REF**: Via_Stitch_Dia0.356mm_Drill0.254mm, Misc:Via_Stitch_Dia0.356mm_Drill0.254mm, F.Cu at (150.3, 60.6)
- added REF**: Via_Stitch_Dia0.356mm_Drill0.254mm, Misc:Via_Stitch_Dia0.356mm_Drill0.254mm, F.Cu at (155.4, 60.6)
- added REF**: Via_Stitch_Dia0.356mm_Drill0.254mm, Misc:Via_Stitch_Dia0.356mm_Drill0.254mm, F.Cu at (158.0, 60.6)
- added REF**: Via_Stitch_Dia0.356mm_Drill0.254mm, Misc:Via_Stitch_Dia0.356mm_Drill0.254mm, F.Cu at (158.0, 63.1)
- added REF**: Via_Stitch_Dia0.356mm_Drill0.254mm, Misc:Via_Stitch_Dia0.356mm_Drill0.254mm, F.Cu at (170.7, 124.1)
- added REF**: Via_Stitch_Dia0.356mm_Drill0.254mm, Misc:Via_Stitch_Dia0.356mm_Drill0.254mm, F.Cu at (155.4, 63.1)
- added REF**: Via_Stitch_Dia0.356mm_Drill0.254mm, Misc:Via_Stitch_Dia0.356mm_Drill0.254mm, F.Cu at (150.3, 63.1)
- added REF**: Via_Stitch_Dia0.356mm_Drill0.254mm, Misc:Via_Stitch_Dia0.356mm_Drill0.254mm, F.Cu at (152.9, 63.1)
- added REF**: Via_Stitch_Dia0.356mm_Drill0.254mm, Misc:Via_Stitch_Dia0.356mm_Drill0.254mm, F.Cu at (142.7, 63.1)
- added REF**: Via_Stitch_Dia0.356mm_Drill0.254mm, Misc:Via_Stitch_Dia0.356mm_Drill0.254mm, F.Cu at (145.3, 63.1)
- added REF**: Via_Stitch_Dia0.356mm_Drill0.254mm, Misc:Via_Stitch_Dia0.356mm_Drill0.254mm, F.Cu at (147.8, 63.1)
- added REF**: Via_Stitch_Dia0.356mm_Drill0.254mm, Misc:Via_Stitch_Dia0.356mm_Drill0.254mm, F.Cu at (163.0, 63.1)
- added REF**: Via_Stitch_Dia0.356mm_Drill0.254mm, Misc:Via_Stitch_Dia0.356mm_Drill0.254mm, F.Cu at (160.5, 63.1)
- added REF**: Via_Stitch_Dia0.356mm_Drill0.254mm, Misc:Via_Stitch_Dia0.356mm_Drill0.254mm, F.Cu at (165.6, 63.1)
- added REF**: Via_Stitch_Dia0.356mm_Drill0.254mm, Misc:Via_Stitch_Dia0.356mm_Drill0.254mm, F.Cu at (168.1, 63.1)
- added REF**: Via_Stitch_Dia0.356mm_Drill0.254mm, Misc:Via_Stitch_Dia0.356mm_Drill0.254mm, F.Cu at (173.2, 124.1)
- added REF**: Via_Stitch_Dia0.356mm_Drill0.254mm, Misc:Via_Stitch_Dia0.356mm_Drill0.254mm, F.Cu at (170.7, 63.1)
- added REF**: Via_Stitch_Dia0.356mm_Drill0.254mm, Misc:Via_Stitch_Dia0.356mm_Drill0.254mm, F.Cu at (170.7, 58.0)
- added REF**: Via_Stitch_Dia0.356mm_Drill0.254mm, Misc:Via_Stitch_Dia0.356mm_Drill0.254mm, F.Cu at (168.1, 58.0)
- added REF**: Via_Stitch_Dia0.356mm_Drill0.254mm, Misc:Via_Stitch_Dia0.356mm_Drill0.254mm, F.Cu at (165.6, 58.0)
- added REF**: Via_Stitch_Dia0.356mm_Drill0.254mm, Misc:Via_Stitch_Dia0.356mm_Drill0.254mm, F.Cu at (160.5, 58.0)
- added REF**: Via_Stitch_Dia0.356mm_Drill0.254mm, Misc:Via_Stitch_Dia0.356mm_Drill0.254mm, F.Cu at (163.0, 58.0)
- added REF**: Via_Stitch_Dia0.356mm_Drill0.254mm, Misc:Via_Stitch_Dia0.356mm_Drill0.254mm, F.Cu at (147.8, 58.0)
- added REF**: Via_Stitch_Dia0.356mm_Drill0.254mm, Misc:Via_Stitch_Dia0.356mm_Drill0.254mm, F.Cu at (145.3, 58.0)
- added REF**: Via_Stitch_Dia0.356mm_Drill0.254mm, Misc:Via_Stitch_Dia0.356mm_Drill0.254mm, F.Cu at (140.2, 58.0)
- added REF**: Via_Stitch_Dia0.356mm_Drill0.254mm, Misc:Via_Stitch_Dia0.356mm_Drill0.254mm, F.Cu at (142.7, 58.0)
- added REF**: Via_Stitch_Dia0.356mm_Drill0.254mm, Misc:Via_Stitch_Dia0.356mm_Drill0.254mm, F.Cu at (173.2, 126.6)
- added REF**: Via_Stitch_Dia0.356mm_Drill0.254mm, Misc:Via_Stitch_Dia0.356mm_Drill0.254mm, F.Cu at (152.9, 58.0)
- added REF**: Via_Stitch_Dia0.356mm_Drill0.254mm, Misc:Via_Stitch_Dia0.356mm_Drill0.254mm, F.Cu at (150.3, 58.0)
- added REF**: Via_Stitch_Dia0.356mm_Drill0.254mm, Misc:Via_Stitch_Dia0.356mm_Drill0.254mm, F.Cu at (155.4, 58.0)
- added REF**: Via_Stitch_Dia0.356mm_Drill0.254mm, Misc:Via_Stitch_Dia0.356mm_Drill0.254mm, F.Cu at (158.0, 58.0)
- added REF**: Via_Stitch_Dia0.356mm_Drill0.254mm, Misc:Via_Stitch_Dia0.356mm_Drill0.254mm, F.Cu at (170.7, 47.9)
- added REF**: Via_Stitch_Dia0.356mm_Drill0.254mm, Misc:Via_Stitch_Dia0.356mm_Drill0.254mm, F.Cu at (168.1, 47.9)
- added REF**: Via_Stitch_Dia0.356mm_Drill0.254mm, Misc:Via_Stitch_Dia0.356mm_Drill0.254mm, F.Cu at (165.6, 47.9)
- added REF**: Via_Stitch_Dia0.356mm_Drill0.254mm, Misc:Via_Stitch_Dia0.356mm_Drill0.254mm, F.Cu at (160.5, 47.9)
- added REF**: Via_Stitch_Dia0.356mm_Drill0.254mm, Misc:Via_Stitch_Dia0.356mm_Drill0.254mm, F.Cu at (163.0, 47.9)
- added REF**: Via_Stitch_Dia0.356mm_Drill0.254mm, Misc:Via_Stitch_Dia0.356mm_Drill0.254mm, F.Cu at (147.8, 47.9)
- added REF**: Via_Stitch_Dia0.356mm_Drill0.254mm, Misc:Via_Stitch_Dia0.356mm_Drill0.254mm, F.Cu at (173.2, 121.5)
- added REF**: Via_Stitch_Dia0.356mm_Drill0.254mm, Misc:Via_Stitch_Dia0.356mm_Drill0.254mm, F.Cu at (145.3, 47.9)
- added REF**: Via_Stitch_Dia0.356mm_Drill0.254mm, Misc:Via_Stitch_Dia0.356mm_Drill0.254mm, F.Cu at (140.2, 47.9)
- added REF**: Via_Stitch_Dia0.356mm_Drill0.254mm, Misc:Via_Stitch_Dia0.356mm_Drill0.254mm, F.Cu at (142.7, 47.9)
- added REF**: Via_Stitch_Dia0.356mm_Drill0.254mm, Misc:Via_Stitch_Dia0.356mm_Drill0.254mm, F.Cu at (152.9, 47.9)
- added REF**: Via_Stitch_Dia0.356mm_Drill0.254mm, Misc:Via_Stitch_Dia0.356mm_Drill0.254mm, F.Cu at (150.3, 47.9)
- added REF**: Via_Stitch_Dia0.356mm_Drill0.254mm, Misc:Via_Stitch_Dia0.356mm_Drill0.254mm, F.Cu at (155.4, 47.9)
- added REF**: Via_Stitch_Dia0.356mm_Drill0.254mm, Misc:Via_Stitch_Dia0.356mm_Drill0.254mm, F.Cu at (158.0, 47.9)
- added REF**: Via_Stitch_Dia0.356mm_Drill0.254mm, Misc:Via_Stitch_Dia0.356mm_Drill0.254mm, F.Cu at (158.0, 50.4)
- added REF**: Via_Stitch_Dia0.356mm_Drill0.254mm, Misc:Via_Stitch_Dia0.356mm_Drill0.254mm, F.Cu at (155.4, 50.4)
- added REF**: Via_Stitch_Dia0.356mm_Drill0.254mm, Misc:Via_Stitch_Dia0.356mm_Drill0.254mm, F.Cu at (150.3, 50.4)
- added REF**: Via_Stitch_Dia0.356mm_Drill0.254mm, Misc:Via_Stitch_Dia0.356mm_Drill0.254mm, F.Cu at (173.2, 119.0)
- added REF**: Via_Stitch_Dia0.356mm_Drill0.254mm, Misc:Via_Stitch_Dia0.356mm_Drill0.254mm, F.Cu at (152.9, 50.4)
- added REF**: Via_Stitch_Dia0.356mm_Drill0.254mm, Misc:Via_Stitch_Dia0.356mm_Drill0.254mm, F.Cu at (142.7, 50.4)
- added REF**: Via_Stitch_Dia0.356mm_Drill0.254mm, Misc:Via_Stitch_Dia0.356mm_Drill0.254mm, F.Cu at (140.2, 50.4)
- added REF**: Via_Stitch_Dia0.356mm_Drill0.254mm, Misc:Via_Stitch_Dia0.356mm_Drill0.254mm, F.Cu at (145.3, 50.4)
- added REF**: Via_Stitch_Dia0.356mm_Drill0.254mm, Misc:Via_Stitch_Dia0.356mm_Drill0.254mm, F.Cu at (147.8, 50.4)
- added REF**: Via_Stitch_Dia0.356mm_Drill0.254mm, Misc:Via_Stitch_Dia0.356mm_Drill0.254mm, F.Cu at (163.0, 50.4)
- added REF**: Via_Stitch_Dia0.356mm_Drill0.254mm, Misc:Via_Stitch_Dia0.356mm_Drill0.254mm, F.Cu at (160.5, 50.4)
- added REF**: Via_Stitch_Dia0.356mm_Drill0.254mm, Misc:Via_Stitch_Dia0.356mm_Drill0.254mm, F.Cu at (165.6, 50.4)
- added REF**: Via_Stitch_Dia0.356mm_Drill0.254mm, Misc:Via_Stitch_Dia0.356mm_Drill0.254mm, F.Cu at (168.1, 50.4)
- added REF**: Via_Stitch_Dia0.356mm_Drill0.254mm, Misc:Via_Stitch_Dia0.356mm_Drill0.254mm, F.Cu at (170.7, 50.4)
- added REF**: Via_Stitch_Dia0.356mm_Drill0.254mm, Misc:Via_Stitch_Dia0.356mm_Drill0.254mm, F.Cu at (165.6, 119.0)
- added REF**: Via_Stitch_Dia0.356mm_Drill0.254mm, Misc:Via_Stitch_Dia0.356mm_Drill0.254mm, F.Cu at (170.7, 55.5)
- added REF**: Via_Stitch_Dia0.356mm_Drill0.254mm, Misc:Via_Stitch_Dia0.356mm_Drill0.254mm, F.Cu at (168.1, 55.5)
- added REF**: Via_Stitch_Dia0.356mm_Drill0.254mm, Misc:Via_Stitch_Dia0.356mm_Drill0.254mm, F.Cu at (165.6, 55.5)
- added REF**: Via_Stitch_Dia0.356mm_Drill0.254mm, Misc:Via_Stitch_Dia0.356mm_Drill0.254mm, F.Cu at (160.5, 55.5)
- added REF**: Via_Stitch_Dia0.356mm_Drill0.254mm, Misc:Via_Stitch_Dia0.356mm_Drill0.254mm, F.Cu at (163.0, 55.5)
- added REF**: Via_Stitch_Dia0.356mm_Drill0.254mm, Misc:Via_Stitch_Dia0.356mm_Drill0.254mm, F.Cu at (147.8, 55.5)
- added REF**: Via_Stitch_Dia0.356mm_Drill0.254mm, Misc:Via_Stitch_Dia0.356mm_Drill0.254mm, F.Cu at (145.3, 55.5)
- added REF**: Via_Stitch_Dia0.356mm_Drill0.254mm, Misc:Via_Stitch_Dia0.356mm_Drill0.254mm, F.Cu at (140.2, 55.5)
- added REF**: Via_Stitch_Dia0.356mm_Drill0.254mm, Misc:Via_Stitch_Dia0.356mm_Drill0.254mm, F.Cu at (142.7, 55.5)
- added REF**: Via_Stitch_Dia0.356mm_Drill0.254mm, Misc:Via_Stitch_Dia0.356mm_Drill0.254mm, F.Cu at (152.9, 55.5)
- added REF**: Via_Stitch_Dia0.356mm_Drill0.254mm, Misc:Via_Stitch_Dia0.356mm_Drill0.254mm, F.Cu at (163.0, 119.0)
- added REF**: Via_Stitch_Dia0.356mm_Drill0.254mm, Misc:Via_Stitch_Dia0.356mm_Drill0.254mm, F.Cu at (150.3, 55.5)
- added REF**: Via_Stitch_Dia0.356mm_Drill0.254mm, Misc:Via_Stitch_Dia0.356mm_Drill0.254mm, F.Cu at (155.4, 55.5)
- added REF**: Via_Stitch_Dia0.356mm_Drill0.254mm, Misc:Via_Stitch_Dia0.356mm_Drill0.254mm, F.Cu at (158.0, 55.5)
- added REF**: Via_Stitch_Dia0.356mm_Drill0.254mm, Misc:Via_Stitch_Dia0.356mm_Drill0.254mm, F.Cu at (158.0, 53.0)
- added REF**: Via_Stitch_Dia0.356mm_Drill0.254mm, Misc:Via_Stitch_Dia0.356mm_Drill0.254mm, F.Cu at (155.4, 53.0)
- added REF**: Via_Stitch_Dia0.356mm_Drill0.254mm, Misc:Via_Stitch_Dia0.356mm_Drill0.254mm, F.Cu at (150.3, 53.0)
- added REF**: Via_Stitch_Dia0.356mm_Drill0.254mm, Misc:Via_Stitch_Dia0.356mm_Drill0.254mm, F.Cu at (152.9, 53.0)
- added REF**: Via_Stitch_Dia0.356mm_Drill0.254mm, Misc:Via_Stitch_Dia0.356mm_Drill0.254mm, F.Cu at (142.7, 53.0)
- added REF**: Via_Stitch_Dia0.356mm_Drill0.254mm, Misc:Via_Stitch_Dia0.356mm_Drill0.254mm, F.Cu at (140.2, 53.0)
- added REF**: Via_Stitch_Dia0.356mm_Drill0.254mm, Misc:Via_Stitch_Dia0.356mm_Drill0.254mm, F.Cu at (145.3, 53.0)
- added REF**: Via_Stitch_Dia0.356mm_Drill0.254mm, Misc:Via_Stitch_Dia0.356mm_Drill0.254mm, F.Cu at (168.1, 119.0)
- added REF**: Via_Stitch_Dia0.356mm_Drill0.254mm, Misc:Via_Stitch_Dia0.356mm_Drill0.254mm, F.Cu at (147.8, 53.0)
- added REF**: Via_Stitch_Dia0.356mm_Drill0.254mm, Misc:Via_Stitch_Dia0.356mm_Drill0.254mm, F.Cu at (163.0, 53.0)
- added REF**: Via_Stitch_Dia0.356mm_Drill0.254mm, Misc:Via_Stitch_Dia0.356mm_Drill0.254mm, F.Cu at (160.5, 53.0)
- added REF**: Via_Stitch_Dia0.356mm_Drill0.254mm, Misc:Via_Stitch_Dia0.356mm_Drill0.254mm, F.Cu at (165.6, 53.0)
- added REF**: Via_Stitch_Dia0.356mm_Drill0.254mm, Misc:Via_Stitch_Dia0.356mm_Drill0.254mm, F.Cu at (168.1, 53.0)
- added REF**: Via_Stitch_Dia0.356mm_Drill0.254mm, Misc:Via_Stitch_Dia0.356mm_Drill0.254mm, F.Cu at (170.7, 53.0)
- added REF**: Via_Stitch_Dia0.356mm_Drill0.254mm, Misc:Via_Stitch_Dia0.356mm_Drill0.254mm, F.Cu at (170.7, 42.8)
- added REF**: Via_Stitch_Dia0.356mm_Drill0.254mm, Misc:Via_Stitch_Dia0.356mm_Drill0.254mm, F.Cu at (168.1, 42.8)
- added REF**: Via_Stitch_Dia0.356mm_Drill0.254mm, Misc:Via_Stitch_Dia0.356mm_Drill0.254mm, F.Cu at (165.6, 42.8)
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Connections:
- DS1 pad 17: (no net) -> GND
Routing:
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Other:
- board text added: "+3V"
- board text added: "+5V"
- board text added: "1"
- board text added: "16"
- board text added: "<- ->"
- board text added: "AUDIO"
- board text added: "April 9, 2017"
- board text added: "BTN"
- board text added: "TOP"
- board text removed: "March 30, 2017"
